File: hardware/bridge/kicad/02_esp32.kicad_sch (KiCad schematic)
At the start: 5 parts, among them U11 ESP32-S3-WROOM-1-N8R2

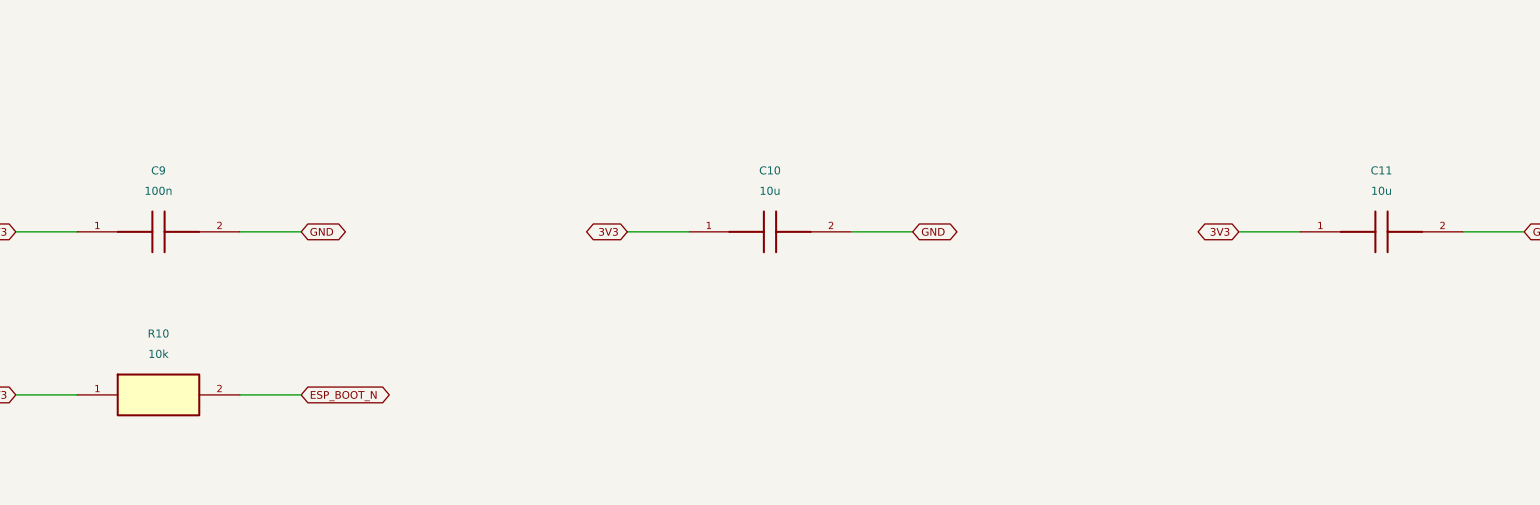
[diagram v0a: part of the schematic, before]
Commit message: fix: close hardware rail-fault paths and sensor contract gaps
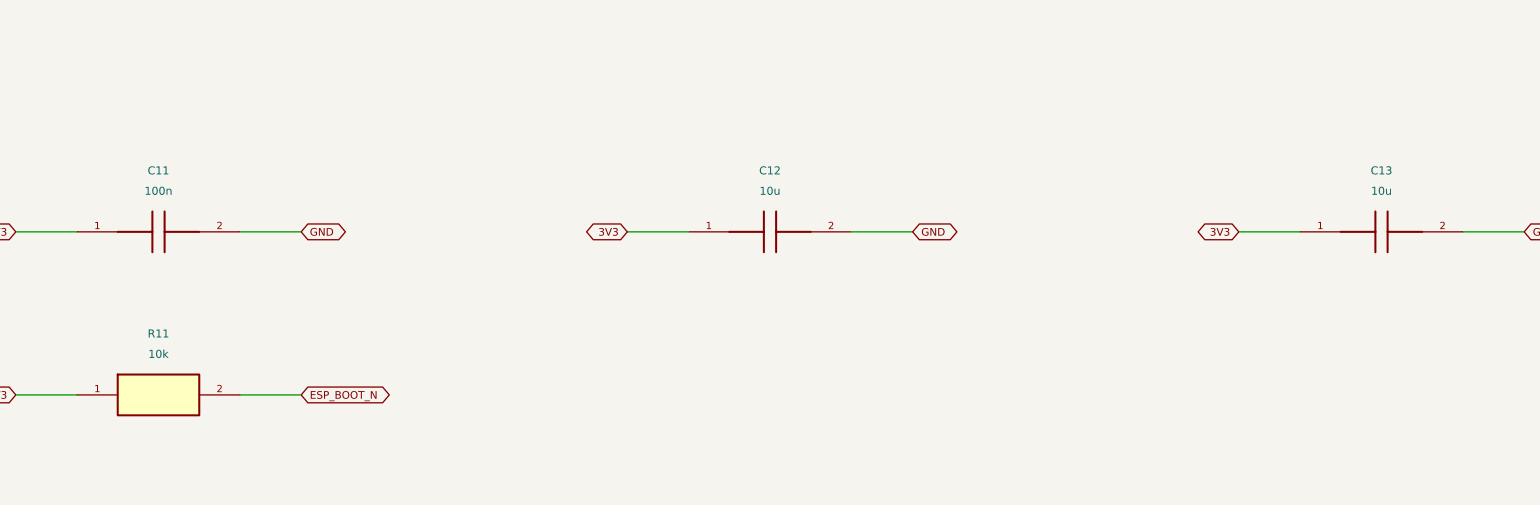
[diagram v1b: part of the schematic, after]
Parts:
- removed C10: 10u, CANView:Capacitor_SMD__C_0603_1608Metric, symbol CANView:CANView_bridge_C10
- removed C9: 100n, CANView:Capacitor_SMD__C_0603_1608Metric, symbol CANView:CANView_bridge_C9
- removed R10: 10k, CANView:Resistor_SMD__R_0402_1005Metric, symbol CANView:CANView_bridge_R10
- added C12: 10u, CANView:Capacitor_SMD__C_0603_1608Metric, symbol CANView:CANView_bridge_C12
- added C13: 10u, CANView:Capacitor_SMD__C_0603_1608Metric, symbol CANView:CANView_bridge_C13
- added R11: 10k, CANView:Resistor_SMD__R_0402_1005Metric, symbol CANView:CANView_bridge_R11
- C11: value 10u -> 100n; MPN GEN-C-0603-10u-16V-X7R -> GEN-C-0603-100n-16V-X7R
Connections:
- net 3V3: now also C12.1, C13.1, R11.1
- net ESP_BOOT_N: now also R11.2
- net GND: now also C12.2, C13.2
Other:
- moved on the sheet: C11

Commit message: Design independent OTA recovery and update N16R8 hardware
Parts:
- U11: Source esp32s3-wroom -> esp32s3-wroom: ordering table, pin definitions, R8 reserved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; Specification 8MB flash + 2MB PSRAM; 3.0..3.6V; -40..85C -> 8MiB Quad flash + 2MiB Quad PSRAM; 3.0..3.6V; -40..85C
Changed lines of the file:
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@@
 (kicad_sch (version 20250114) (generator "eeschema") (generator_version "10.0") (paper "A3") (title_block (title "CANView / 02_esp32") (date "2026-09-05") (rev "R1 REVIEW") (company "digitie/canview") (comment 1 "SCHEMATIC REVIEW ONLY - PCB/HIL release gates remain open"))
 (text "ESP32-S3-WROOM-1. Keep antenna clearance. USB native serial/JTAG. PSRAM pins reserved." (at 15.24 15.24 0) (effects (font (size 1.2 1.2)) (justify left)))
-(symbol (lib_id "CANView:CANView_bridge_U11") (at 88.9000 101.6000 0) (unit 1) (in_bom yes) (on_board yes) (dnp no) (property "Reference" "U11" (at 88.9000 40.6400 0)  (effects (font (size 1.0 1.0)) ))(property "Value" "ESP32-S3-WROOM-1-N8R2" (at 88.9000 43.1800 0)  (effects (font (size 1.0 1.0)) ))(property "Footprint" "CANView:RF_Module__ESP32-S3-WROOM-1" (at 88.9000 101.6000 0) (hide yes) (effects (font (size 1.0 1.0)) ))(property "MPN" "ESP32-S3-WROOM-1-N8R2" (at 88.9000 101.6000 0) (hide yes) (effects (font (size 1.0 1.0)) ))(property "Specification" "8MB flash + 2MB PSRAM; 3.0..3.6V; -40..85C" (at 88.9000 101.6000 0) (hide yes) (effects (font (size 1.0 1.0)) ))(property "Source" "esp32s3-wroom" (at 88.9000 101.6000 0) (hide yes) (effects (font (size 1.0 1.0)) ))(property "Assembly" "FIT" (at 88.9000 101.6000 0) (hide yes) (effects (font (size 1.0 1.0)) ))(instances (project "bridge" (path "/695535dc-1835-5369-a035-dbad415d33c6/234d7795-fc3a-5f3e-8372-5430bb736c95" (reference "U11") (unit 1)))))
+(symbol (lib_id "CANView:CANView_bridge_U11") (at 88.9000 101.6000 0) (unit 1) (in_bom yes) (on_board yes) (dnp no) (property "Reference" "U11" (at 88.9000 40.6400 0)  (effects (font (size 1.0 1.0)) ))(property "Value" "ESP32-S3-WROOM-1-N8R2" (at 88.9000 43.1800 0)  (effects (font (size 1.0 1.0)) ))(property "Footprint" "CANView:RF_Module__ESP32-S3-WROOM-1" (at 88.9000 101.6000 0) (hide yes) (effects (font (size 1.0 1.0)) ))(property "MPN" "ESP32-S3-WROOM-1-N8R2" (at 88.9000 101.6000 0) (hide yes) (effects (font (size 1.0 1.0)) ))(property "Specification" "8MiB Quad flash + 2MiB Quad PSRAM; 3.0..3.6V; -40..85C" (at 88.9000 101.6000 0) (hide yes) (effects (font (size 1.0 1.0)) ))(property "Source" "esp32s3-wroom: ordering table, pin definitions, R8 reserved GPIO35/36/37; PSRAM ECC temperature note" (at 88.9000 101.6000 0) (hide yes) (effects (font (size 1.0 1.0)) ))(property "Assembly" "FIT" (at 88.9000 101.6000 0) (hide yes) (effects (font (size 1.0 1.0)) ))(instances (project "bridge" (path "/695535dc-1835-5369-a035-dbad415d33c6/234d7795-fc3a-5f3e-8372-5430bb736c95" (reference "U11") (unit 1)))))
 (wire (pts (xy 63.5000 50.8000) (xy 55.8800 50.8000)) (stroke (width 0) (type default)))
 (global_label "GND" (shape bidirectional) (at 55.8800 50.8000 180) (effects (font (size 0.95 0.95)) (justify right)) (property "Intersheetrefs" "${INTERSHEET_REFS}" (at 55.8800 50.8000 0) (hide yes) (effects (font (size 1.0 1.0)) )))
